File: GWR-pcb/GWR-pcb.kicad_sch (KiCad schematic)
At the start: 46 parts, among them J1 Conn_01x04, J2 Conn_01x11, J3 Conn_01x10, J4 Conn_01x10, J5 Conn_01x12, M1 Motor_DC, Q1 AO3400A, SW1 SW_DIP_x01, U1 AMS1117-1.5, U2 XIAO-ESP32-S3-Plus-SMD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

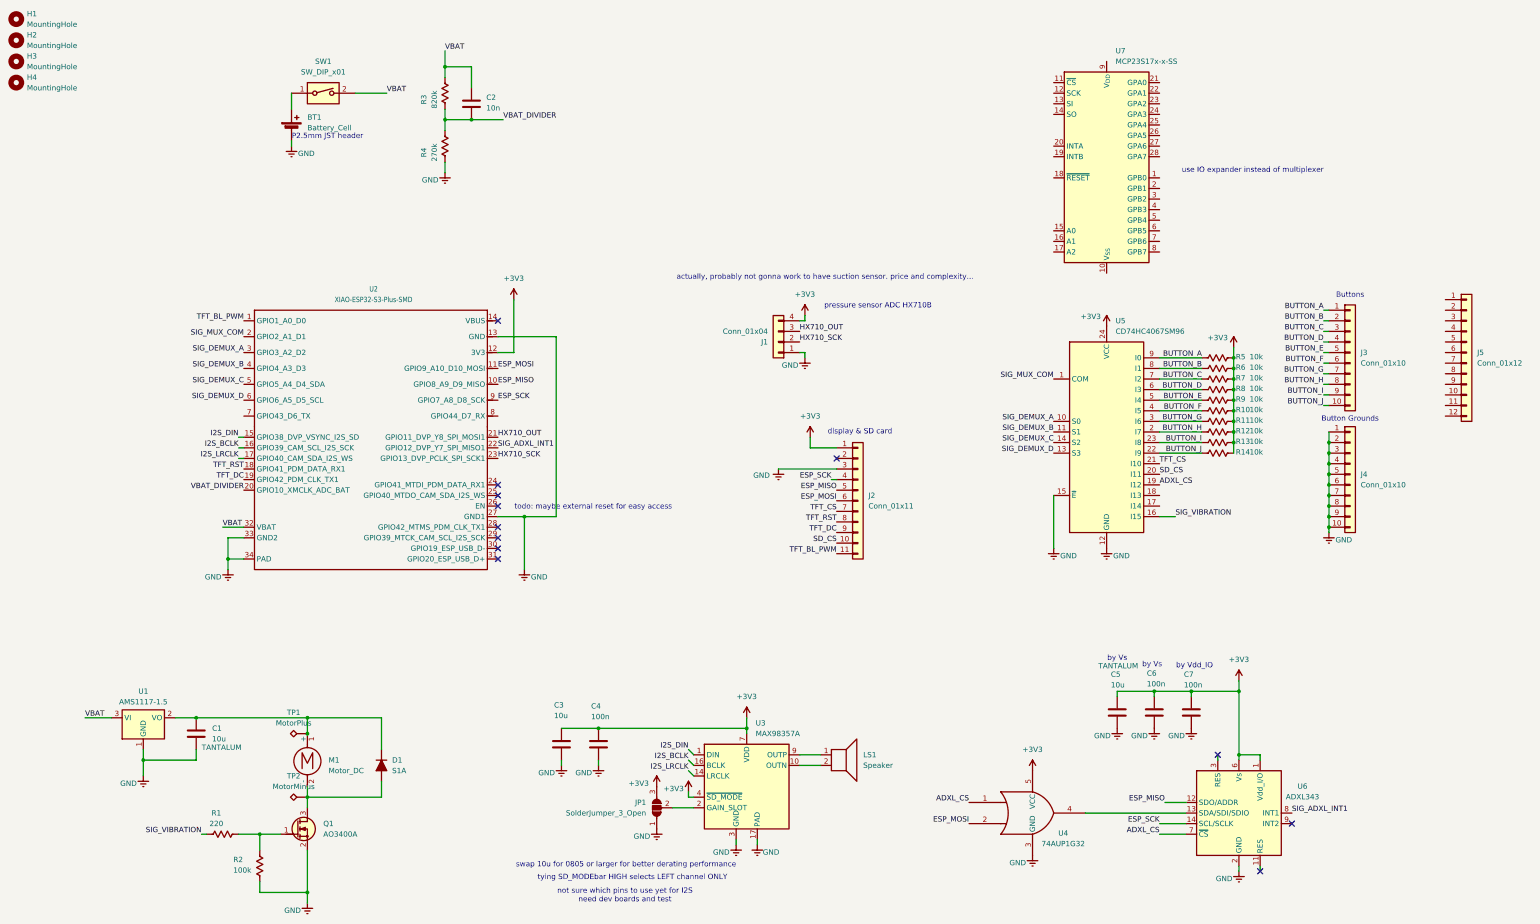
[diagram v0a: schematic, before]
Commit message: update to use GPIO expander, minor fixes
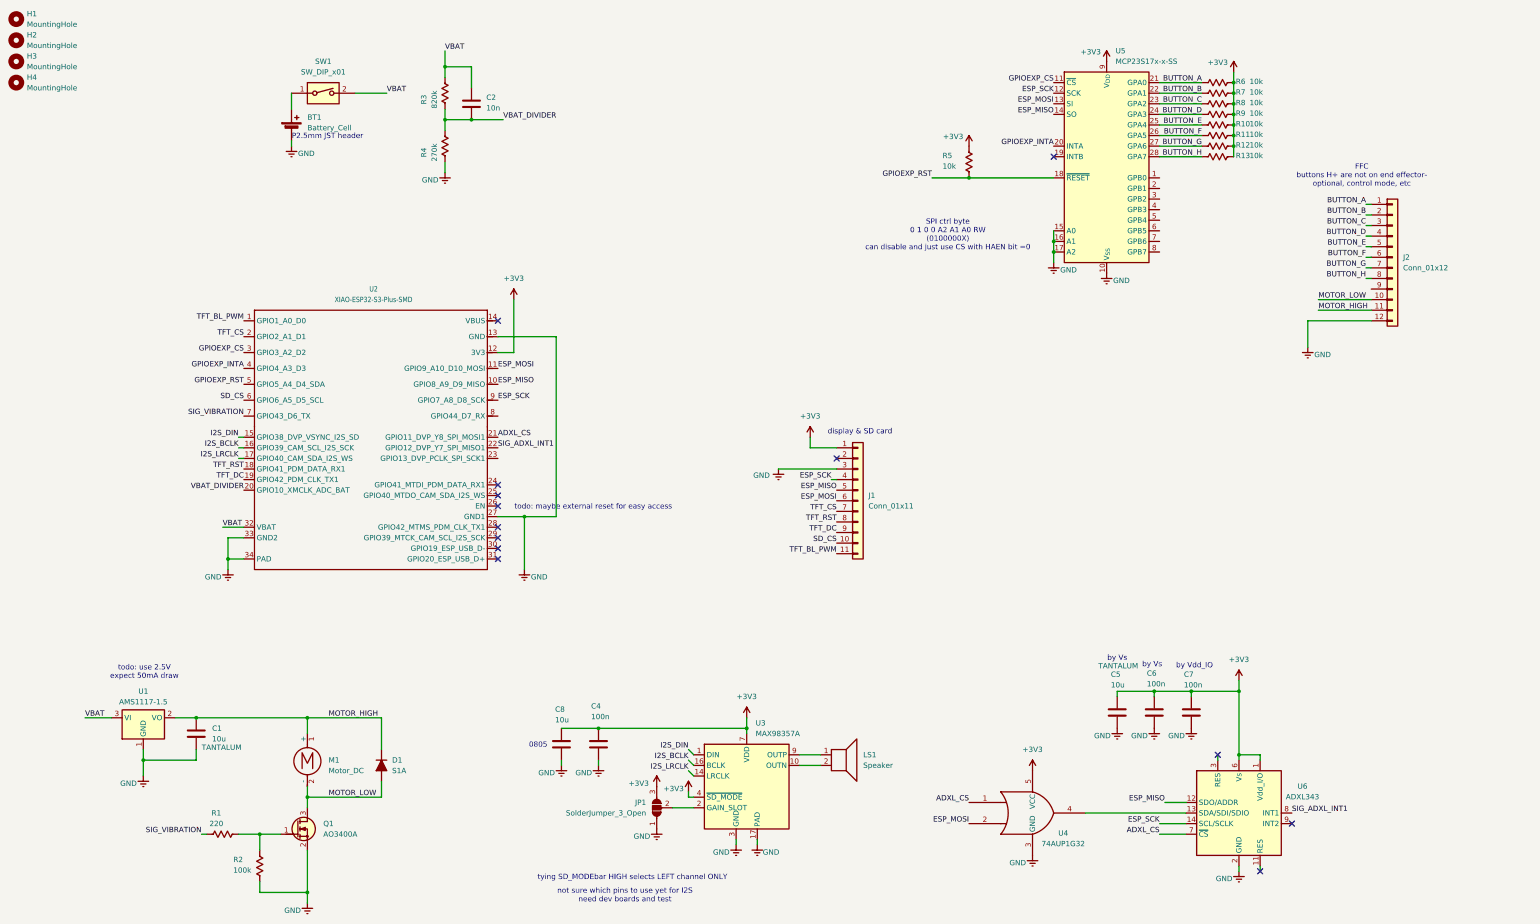
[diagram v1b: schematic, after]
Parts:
- removed C3: 10u, Capacitor_SMD:C_0603_1608Metric, symbol Device:C
- removed J1: Conn_01x04, Connector_PinHeader_2.54mm:PinHeader_1x04_P2.54mm_Vertical, symbol Connector_Generic:Conn_01x04
- removed J3, J4: Conn_01x10, Connector_PinSocket_1.27mm:PinSocket_1x10_P1.27mm_Vertical, symbol Connector_Generic:Conn_01x10
- removed R14: 10k, Resistor_SMD:R_0603_1608Metric_Pad0.98x0.95mm_HandSolder, symbol PCM_Resistor_US_AKL:R_0603
- removed TP1: MotorPlus, Connector_Wire:SolderWire-0.127sqmm_1x01_D0.48mm_OD1mm, symbol Connector:TestPoint_Alt
- removed TP2: MotorMinus, Connector_Wire:SolderWire-0.127sqmm_1x01_D0.48mm_OD1mm, symbol Connector:TestPoint_Alt
- removed U5: CD74HC4067SM96, Package_SO:SSOP-24_5.3x8.2mm_P0.65mm, symbol 74xx:CD74HC4067SM
- added C8: 10u, Capacitor_SMD:C_0805_2012Metric, symbol PCM_Capacitor_AKL:C_0805
- renumbered J2 to J1, J5 to J2, U7 to U5
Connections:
- net BUTTON_I is gone; now on net BUTTON_H: R13.2
- net HX710_OUT is gone; now on net ADXL_CS: U2.21 (GPIO11_DVP_Y8_SPI_MOSI1)
- net SIG_DEMUX_A is gone; now on net GPIOEXP_CS: U2.3 (GPIO3_A2_D2)
- net SIG_DEMUX_B is gone; now on net GPIOEXP_INTA: U2.4 (GPIO4_A3_D3)
- net SIG_DEMUX_C is gone; now on net GPIOEXP_RST: U2.5 (GPIO5_A4_D4_SDA)
- net SIG_DEMUX_D is gone; now on net SD_CS: U2.6 (GPIO6_A5_D5_SCL)
- net SIG_MUX_COM is gone; now on net TFT_CS: U2.2 (GPIO2_A1_D1)
- net +3V3: now also U5.9 (V_{DD}), C8.1
- net BUTTON_A: now also J2.1 (Pin_1), R6.2, U5.21 (GPA0); no longer R5.2
- net BUTTON_B: now also J2.2 (Pin_2), R7.2, U5.22 (GPA1); no longer R6.2
- net BUTTON_C: now also J2.3 (Pin_3), R8.2, U5.23 (GPA2); no longer R7.2
- net BUTTON_D: now also J2.4 (Pin_4), R9.2, U5.24 (GPA3); no longer R8.2
- net BUTTON_E: now also J2.5 (Pin_5), R10.2, U5.25 (GPA4); no longer R9.2
- net BUTTON_F: now also J2.6 (Pin_6), R11.2, U5.26 (GPA5); no longer R10.2
- net BUTTON_G: now also J2.7 (Pin_7), R12.2, U5.27 (GPA6); no longer R11.2
- net BUTTON_H: now also J2.8 (Pin_8), U5.28 (GPA7); no longer R12.2
- net ESP_MISO: now also U5.14 (SO)
- net ESP_MOSI: now also U5.13 (SI)
- net ESP_SCK: now also U5.12 (SCK)
- net GND: now also J2.12 (Pin_12), U5.10 (V_{SS}), U5.15 (A0), U5.16 (A1), U5.17 (A2), C8.2
- net SIG_VIBRATION: now also U2.7 (GPIO43_D6_TX)
- net MOTOR_HIGH: now reaches C1.1, D1.1 (K), M1.1 (+), U1.2 (VO)
- net MOTOR_HIGH: now also J2.11 (Pin_11)
- net MOTOR_LOW: now reaches D1.2 (A), M1.2 (-), Q1.3 (D)
- net MOTOR_LOW: now also J2.10 (Pin_10)
- net GPIOEXP_CS: now reaches U5.11 (~{CS})
- net GPIOEXP_RST: now reaches U5.18 (~{RESET})
- net GPIOEXP_RST: now also R5.2
- net GPIOEXP_INTA: now reaches U5.20 (INTA)
- net HX710_SCK: no longer names the net of U2.23 (GPIO13_DVP_PCLK_SPI_SCK1)
- no-connect marks 12 -> 13
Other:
- note added: "0805"
- note added: "FFC buttons H+ are not on end effector- optional, control mode, etc"
- note added: "SPI ctrl byte 0 1 0 0 A2 A1 A0 RW (0100000X) can disable and just use CS with HAEN bit =0"
- note added: "todo: use 2.5V expect 50mA draw"
- note removed: "Button Grounds"
- note removed: "Buttons"
- note removed: "actually, probably not gonna work to have suction sensor. price and complexity..."
- note removed: "pressure sensor ADC HX710B"
- note removed: "swap 10u for 0805 or larger for better derating performance"
- note removed: "use IO expander instead of multiplexer"
- moved on the sheet: J2

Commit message: standardize port to match 3D; panelize daughterboard
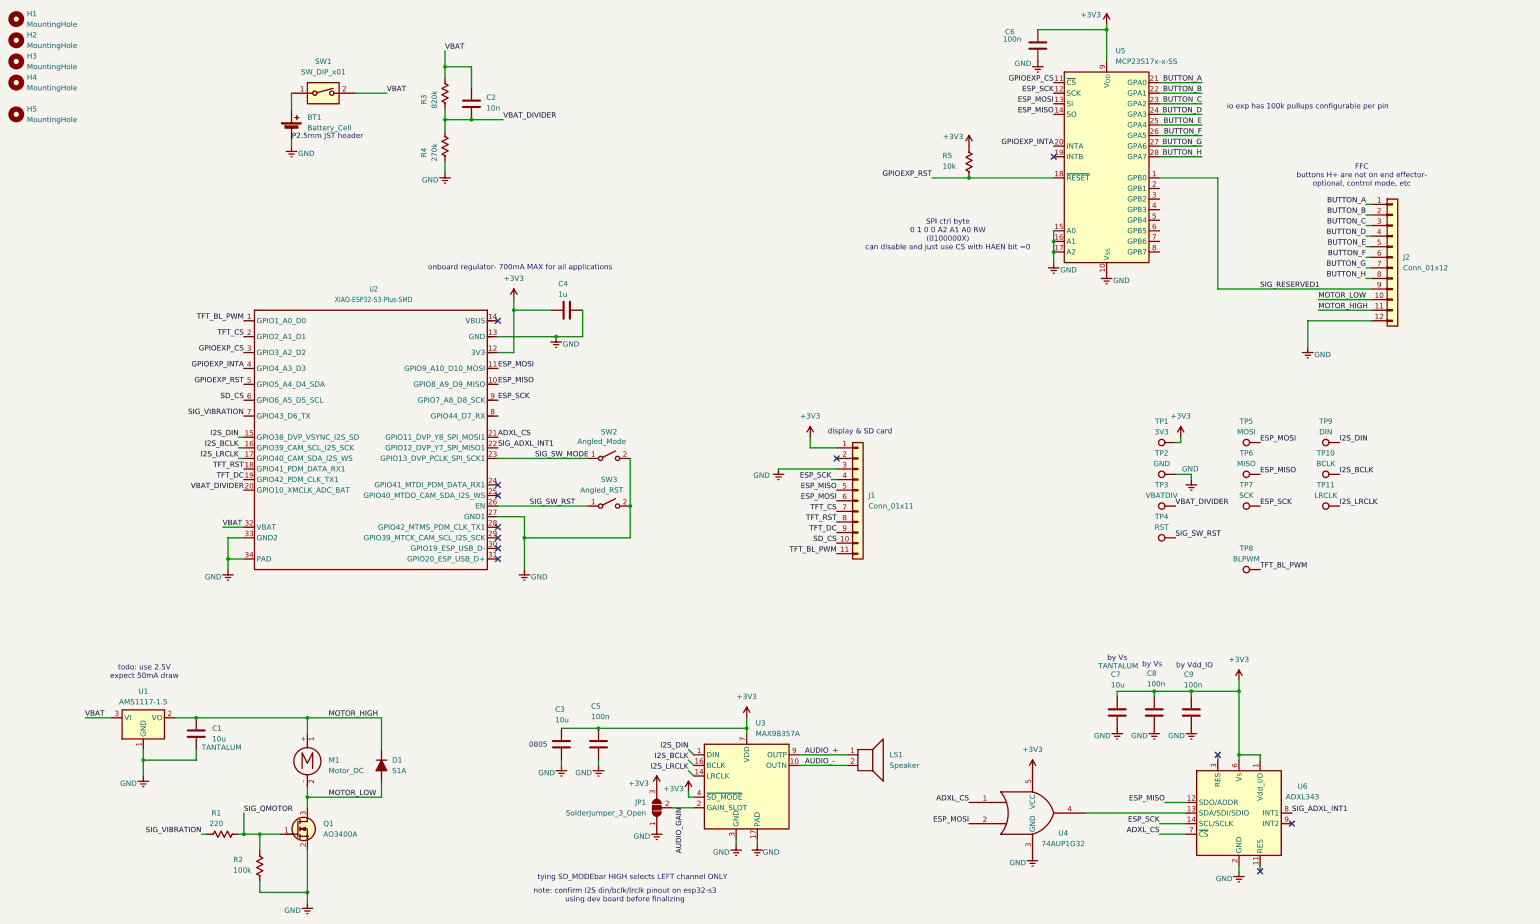
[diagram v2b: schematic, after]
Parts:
- removed R10, R11, R12, R13, R6, R7, R8, R9: 10k, Resistor_SMD:R_0603_1608Metric_Pad0.98x0.95mm_HandSolder, symbol PCM_Resistor_US_AKL:R_0603
- added C4: 1u, Capacitor_SMD:C_0603_1608Metric, symbol Device:C
- added C6: 100n, Capacitor_SMD:C_0603_1608Metric, symbol Device:C
- added H5: MountingHole, MountingHole:MountingHole_3.2mm_M3_DIN965, symbol Mechanical:MountingHole
- added SW2: Angled_Mode, Button_Switch_THT:SW_Tactile_SPST_Angled_PTS645Vx83-2LFS, symbol Switch:SW_SPST
- added SW3: Angled_RST, Button_Switch_THT:SW_Tactile_SPST_Angled_PTS645Vx83-2LFS, symbol Switch:SW_SPST
- added TP1: 3V3, TestPoint:TestPoint_Pad_D1.0mm, symbol Connector:TestPoint
- added TP10: BCLK, TestPoint:TestPoint_Pad_D1.0mm, symbol Connector:TestPoint
- added TP11: LRCLK, TestPoint:TestPoint_Pad_D1.0mm, symbol Connector:TestPoint
- added TP2: GND, TestPoint:TestPoint_Pad_D1.0mm, symbol Connector:TestPoint
- added TP3: VBATDIV, TestPoint:TestPoint_Pad_D1.0mm, symbol Connector:TestPoint
- added TP4: RST, TestPoint:TestPoint_Pad_D1.0mm, symbol Connector:TestPoint
- added TP5: MOSI, TestPoint:TestPoint_Pad_D1.0mm, symbol Connector:TestPoint
- added TP6: MISO, TestPoint:TestPoint_Pad_D1.0mm, symbol Connector:TestPoint
- added TP7: SCK, TestPoint:TestPoint_Pad_D1.0mm, symbol Connector:TestPoint
- added TP8: BLPWM, TestPoint:TestPoint_Pad_D1.0mm, symbol Connector:TestPoint
- added TP9: DIN, TestPoint:TestPoint_Pad_D1.0mm, symbol Connector:TestPoint
- renumbered C8 to C3, C4 to C5, C5 to C7, C6 to C8, C7 to C9
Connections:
- net +3V3: now also C4.1, C6.1, TP1.1
- net ESP_MISO: now also TP6.1
- net ESP_MOSI: now also TP5.1
- net ESP_SCK: now also TP7.1
- net GND: now also C4.2, C6.2, SW2.2 (B), SW3.2 (B), TP2.1
- net I2S_BCLK: now also TP10.1
- net I2S_DIN: now also TP9.1
- net I2S_LRCLK: now also TP11.1
- net TFT_BL_PWM: now also TP8.1
- net VBAT_DIVIDER: now also TP3.1
- net SIG_QMOTOR: now reaches Q1.1 (G), R1.2, R2.1
- net AUDIO_-: now reaches LS1.2, U3.10 (OUTN)
- net AUDIO_GAIN: now reaches JP1.2 (C), U3.2 (GAIN_SLOT)
- net AUDIO_+: now reaches LS1.1, U3.9 (OUTP)
- net SIG_SW_MODE: now reaches U2.23 (GPIO13_DVP_PCLK_SPI_SCK1)
- net SIG_SW_MODE: now also SW2.1 (A)
- net SIG_SW_RST: now reaches U2.26 (EN)
- net SIG_SW_RST: now also SW3.1 (A), TP4.1
- net SIG_RESERVED1: now reaches J2.9 (Pin_9)
- net SIG_RESERVED1: now also U5.1 (GPB0)
- no-connect marks 13 -> 12
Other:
- note added: "io exp has 100k pullups configurable per pin"
- note added: "note: confirm I2S din/bclk/lrclk pinout on esp32-s3 using dev board before finalizing"
- note added: "onboard regulator- 700mA MAX for all applications"
- note removed: "not sure which pins to use yet for I2S need dev boards and test"
- note removed: "todo: maybe external reset for easy access"
- moved on the sheet: LS1
